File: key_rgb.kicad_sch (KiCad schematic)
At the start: 4 parts

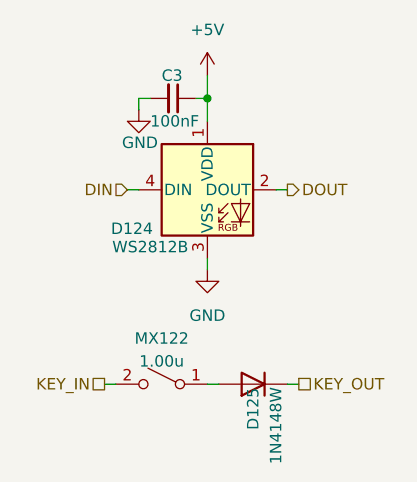
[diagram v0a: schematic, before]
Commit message: Unified key sch pages
One large page is simpler in this case
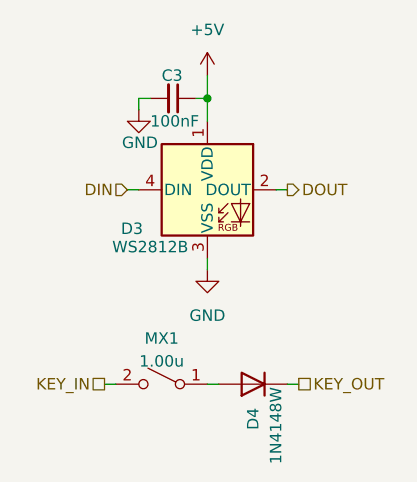
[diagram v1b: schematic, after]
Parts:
- renumbered D124 to D3, D125 to D4, MX122 to MX1

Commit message: RGB LED level shifter. Various components
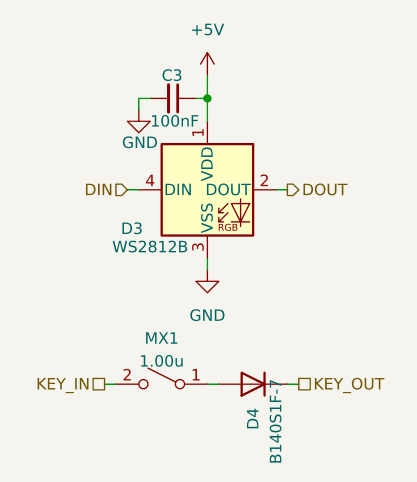
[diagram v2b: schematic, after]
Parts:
- D4: value 1N4148W -> B140S1F-7; footprint keyboard:D_SOD-123 -> Diode_SMD:D_SOD-123F
- MX1: footprint keyboard:SW_Cherry_MX_6.25u_PCB -> key-switches:SW_Gateron_LowProfile_HotSwap_PTH
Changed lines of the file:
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@@
 			)
 		)
-		(property "Footprint" "keyboard:SW_Cherry_MX_6.25u_PCB"
+		(property "Footprint" "key-switches:SW_Gateron_LowProfile_HotSwap_PTH"
 			(at 144.78 114.3 0)
 			(effects
@@
 			)
 		)
-		(property "Value" "1N4148W"
+		(property "Value" "B140S1F-7"
 			(at 157.48 123.19 90)
 			(effects
@@
 			)
 		)
-		(property "Footprint" "keyboard:D_SOD-123"
+		(property "Footprint" "Diode_SMD:D_SOD-123F"
 			(at 154.94 114.3 0)
 			(effects

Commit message: Layout start. Add symbols to proj lib
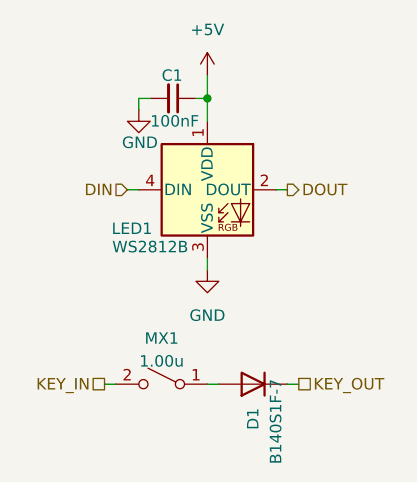
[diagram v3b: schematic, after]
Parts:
- C1: renamed from C3; footprint Capacitor_SMD:C_0603_1608Metric -> Capacitor_SMD:C_0402_1005Metric
- LED1: renamed from D3; symbol LED:WS2812B -> keyboard:WS2812B
- renumbered D4 to D1

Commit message: Status LEDs
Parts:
- C1: footprint Capacitor_SMD:C_0402_1005Metric -> keyboard:C_0402_1005Metric
- D1: footprint Diode_SMD:D_SOD-123F -> keyboard:D_SOD-123F
- LED1: footprint LED_SMD:LED_WS2812B_PLCC4_5.0x5.0mm_P3.2mm -> keyboard:LED_WS2812B-2020_PLCC4_2.0x2.0mm
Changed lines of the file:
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@@
 			)
 		)
-		(property "Footprint" "Capacitor_SMD:C_0402_1005Metric"
+		(property "Footprint" "keyboard:C_0402_1005Metric"
 			(at 146.05 82.55 0)
 			(effects
@@
 			)
 		)
-		(property "Footprint" "Diode_SMD:D_SOD-123F"
+		(property "Footprint" "keyboard:D_SOD-123F"
 			(at 154.94 114.3 0)
 			(effects
@@
 			)
 		)
-		(property "Footprint" "LED_SMD:LED_WS2812B_PLCC4_5.0x5.0mm_P3.2mm"
+		(property "Footprint" "keyboard:LED_WS2812B-2020_PLCC4_2.0x2.0mm"
 			(at 151.13 100.33 0)
 			(effects

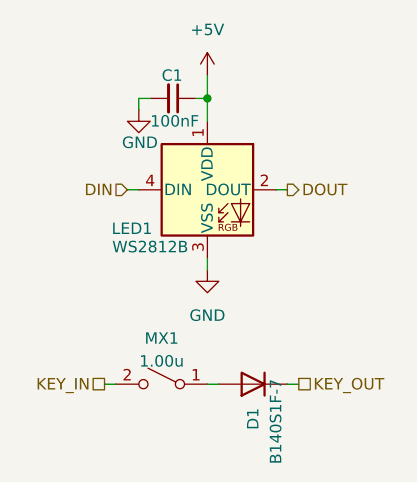
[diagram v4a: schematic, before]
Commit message: Minor sch changes. Work towards matching g915 pcb dimensions
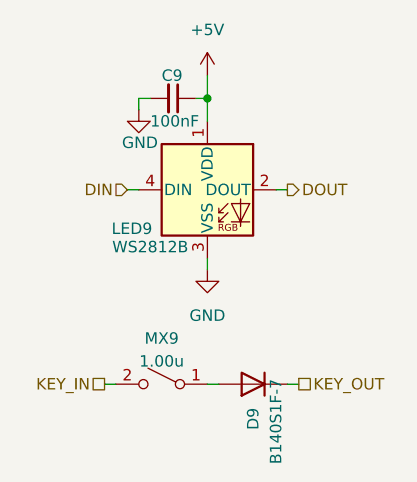
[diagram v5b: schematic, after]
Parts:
- renumbered C1 to C9, D1 to D9, LED1 to LED9, MX1 to MX9
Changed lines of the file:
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@@
 		(on_board yes)
 		(dnp no)
-		(property "Reference" "#PWR01"
+		(property "Reference" "#PWR025"
 			(at 142.24 90.17 0)
 			(effects
@@
 		(dnp no)
 		(fields_autoplaced yes)
-		(property "Reference" "#PWR02"
+		(property "Reference" "#PWR026"
 			(at 149.86 83.82 0)
 			(effects
@@
 		(on_board yes)
 		(dnp no)
-		(property "Reference" "C1"
+		(property "Reference" "C9"
 			(at 144.78 80.01 90)
 			(effects
@@
 		(on_board yes)
 		(dnp no)
-		(property "Reference" "MX1"
+		(property "Reference" "MX9"
 			(at 144.78 109.22 0)
 			(effects
@@
 		(on_board yes)
 		(dnp no)
-		(property "Reference" "D1"
+		(property "Reference" "D9"
 			(at 154.94 119.38 90)
 			(effects
@@
 		(dnp no)
 		(fields_autoplaced yes)
-		(property "Reference" "#PWR03"
+		(property "Reference" "#PWR027"
 			(at 149.86 107.95 0)
 			(effects
@@
 		(on_board yes)
 		(dnp no)
-		(property "Reference" "LED1"
+		(property "Reference" "LED9"
 			(at 141.478 97.028 0)
 			(effects

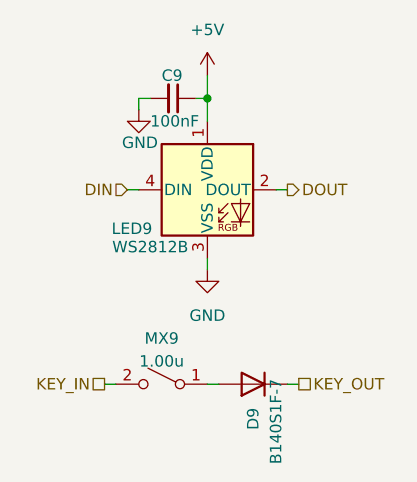
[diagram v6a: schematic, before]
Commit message: Switch to matrix RGB LED
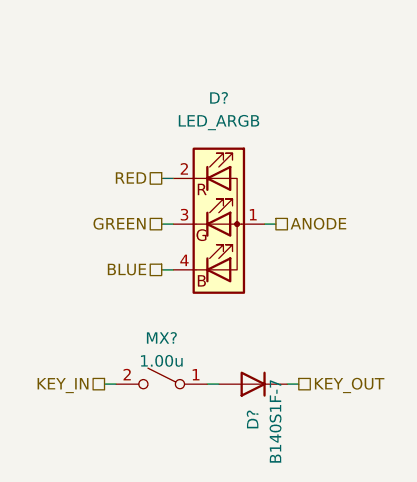
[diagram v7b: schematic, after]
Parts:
- removed C9: 100nF, keyboard:C_0402_1005Metric, symbol Device:C_Small
- removed LED9: WS2812B, keyboard:LED_WS2812B-2020_PLCC4_2.0x2.0mm, symbol keyboard:WS2812B
- added D?: LED_ARGB, symbol Device:LED_ARGB
- renumbered D9 to D?, MX9 to MX?
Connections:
- new net ANODE: D?.1 (A)
- new net BLUE: D?.4 (BK)
- new net GREEN: D?.3 (GK)
- new net RED: D?.2 (RK)
